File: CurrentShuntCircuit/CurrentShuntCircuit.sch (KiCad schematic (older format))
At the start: 48 parts, among them J1 Connection, J2 Connection, J3 Debug/UPDI, J4 Screw_Terminal_01x04, J5 Screw_Terminal_01x04, J6 ScrewTerminal, SW1 SW_DIP_x02, U1 TLP172GM, U2 ATtiny1614-SS, U3 INA228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

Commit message: Updated footprints
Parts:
- SW1: footprint CurrentShuntCircuit:XKBConnectivity_DSHP02TS-S_P1.27 -> Button_Switch_THT:SW_DIP_SPSTx02_Slide_6.7x6.64mm_W7.62mm_P2.54mm_LowProfile; LCSCStockCode C319052 -> C458081
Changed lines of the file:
@@
 F 0 "SW1" H 5835 7067 50  0000 C CNN
 F 1 "SW_DIP_x02" H 5835 6976 50  0000 C CNN
-F 2 "CurrentShuntCircuit:XKBConnectivity_DSHP02TS-S_P1.27" H 5835 6700 50  0001 C CNN
-F 3 "https://datasheet.lcsc.com/szlcsc/2002271742_XKB-Connectivity-DSHP02TS-S_C319052.pdf" H 5835 6700 50  0001 C CNN
-F 4 "C319052" H 5835 6700 50  0001 C CNN "LCSCStockCode"
+F 2 "Button_Switch_THT:SW_DIP_SPSTx02_Slide_6.7x6.64mm_W7.62mm_P2.54mm_LowProfile" H 5835 6700 50  0001 C CNN
+F 3 "https://datasheet.lcsc.com/szlcsc/2004251705_Korean-Hroparts-Elec-DS-02BP_C458081.pdf" H 5835 6700 50  0001 C CNN
+F 4 "C458081" H 5835 6700 50  0001 C CNN "LCSCStockCode"
 	1    5835 6700
 	1    0    0    -1

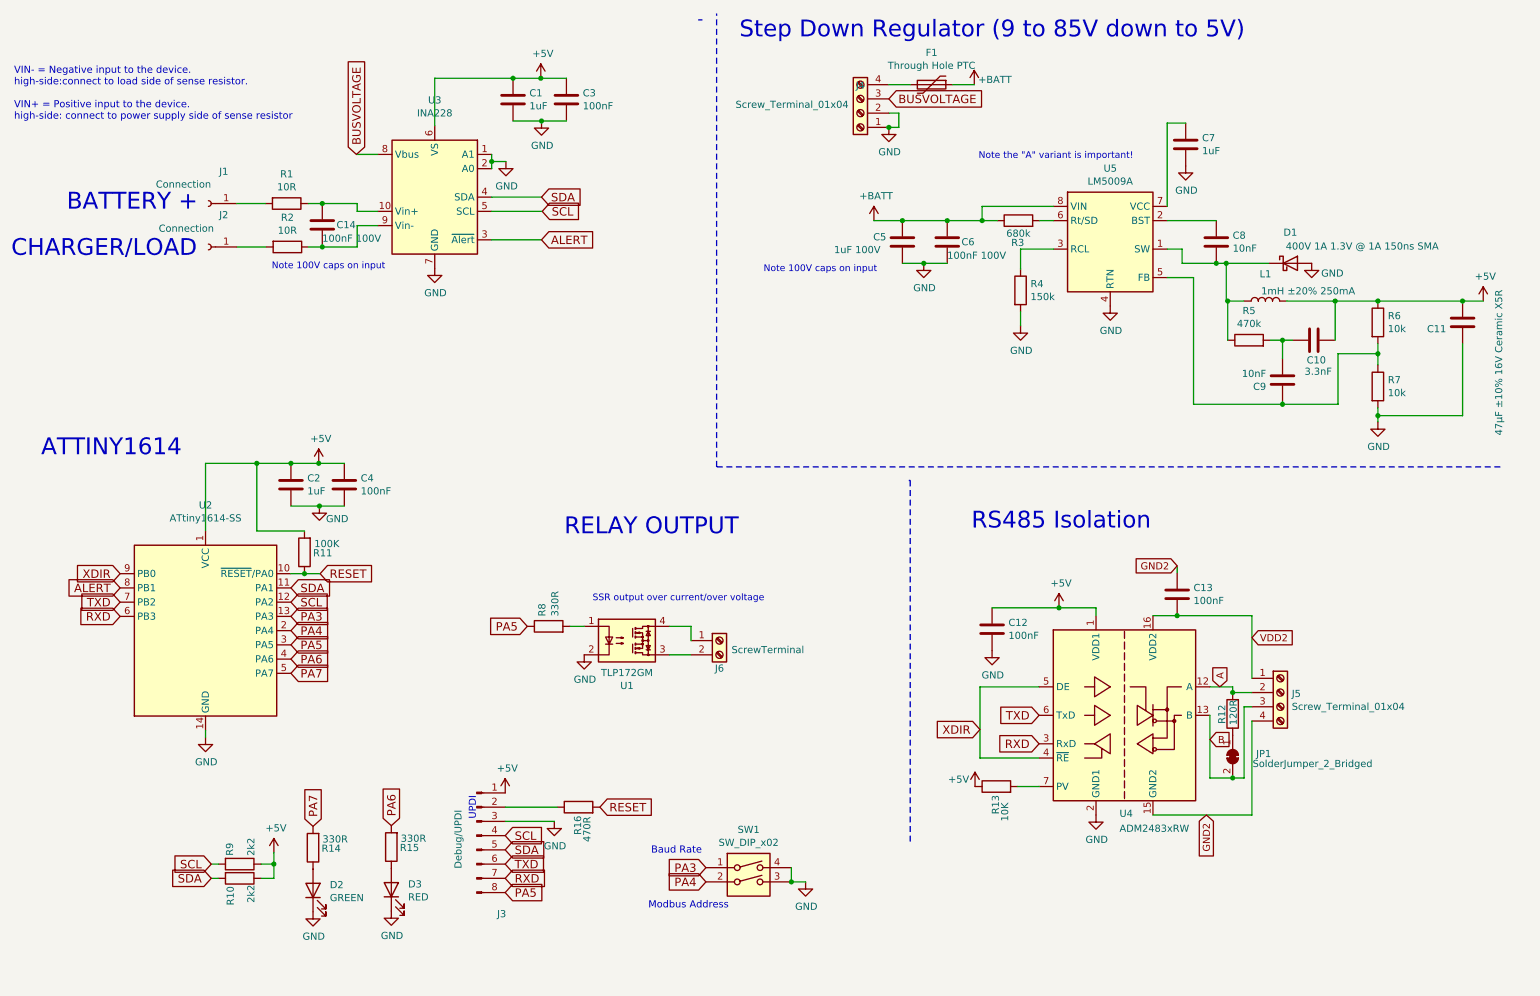
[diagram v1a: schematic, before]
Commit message: Tidy up and change i2c pull ups to 4k7
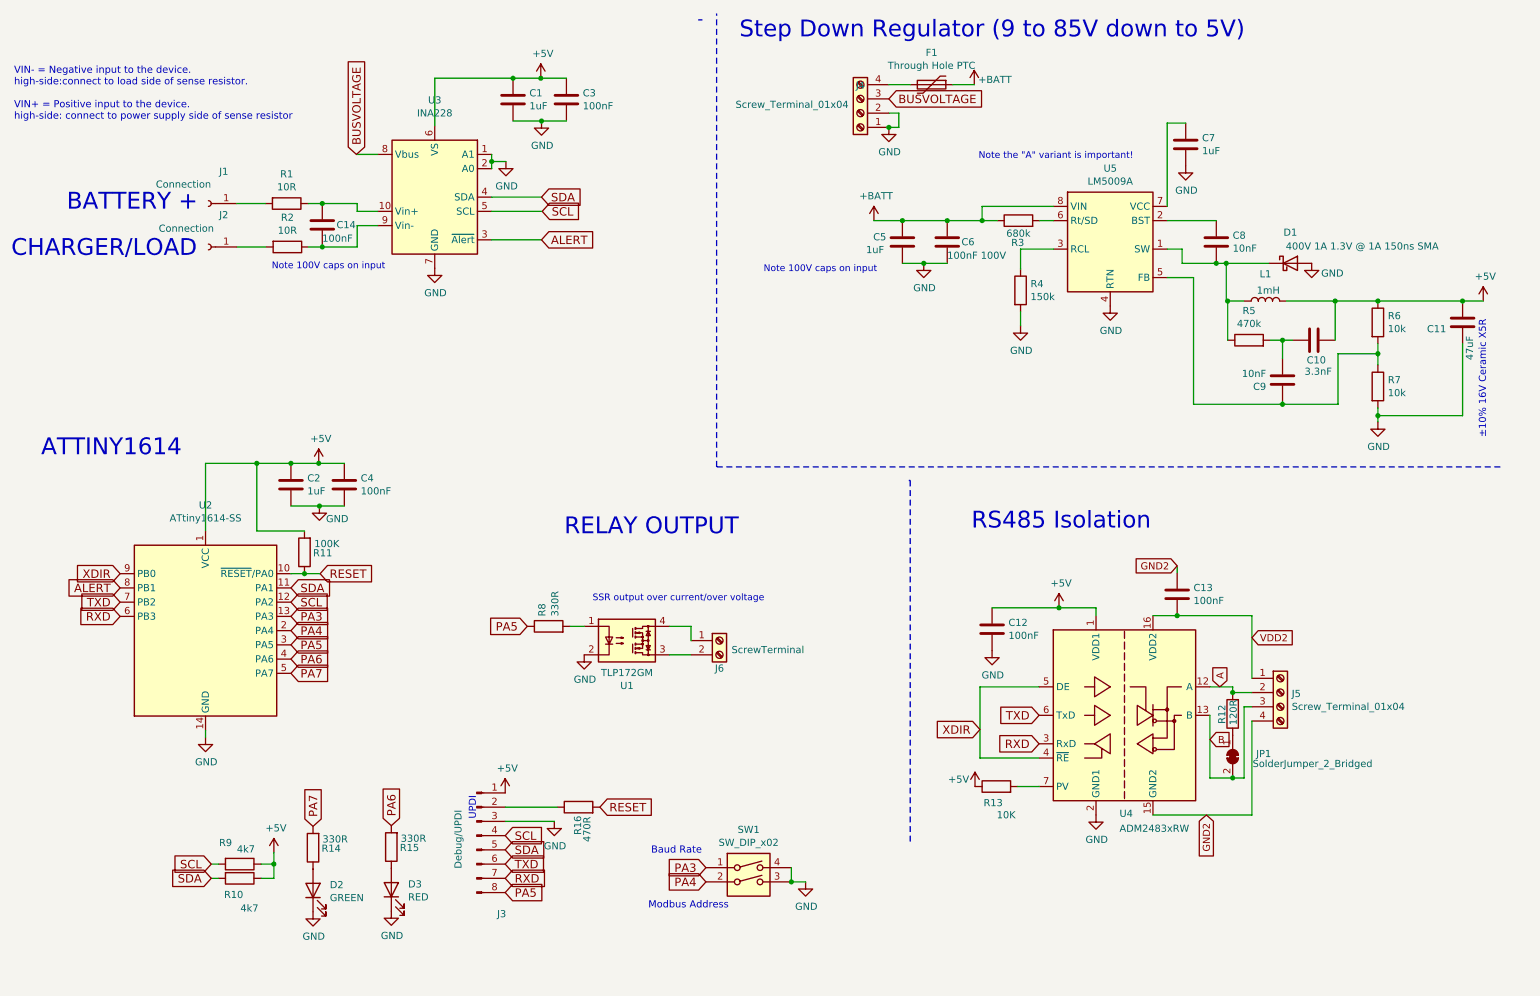
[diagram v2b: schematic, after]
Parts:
- C11: value 47µF ±10% 16V Ceramic X5R -> 47uF
- C14: value 100nF 100V -> 100nF
- C5: value 1uF 100V -> 1uF
- L1: value 1mH ±20% 250mA -> 1mH
- R10, R9: value 2k2 -> 4k7; LCSCStockCode C17520 -> C17673; PartNumber 0805W8F2201T5E -> 0805W8F4701T5E
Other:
- note added: "±10% 16V Ceramic X5R"
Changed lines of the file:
@@
 P 6915 2205
 F 0 "C5" H 6710 2240 50  0000 L CNN
-F 1 "1uF 100V" H 6435 2150 50  0000 L CNN
+F 1 "1uF" H 6660 2150 50  0000 L CNN
 F 2 "Capacitor_SMD:C_1206_3216Metric" H 6953 2055 50  0001 C CNN
 F 3 "https://datasheet.lcsc.com/szlcsc/Samsung-Electro-Mechanics-CL31B105KCHNNNE_C13832.pdf" H 6915 2205 50  0001 C CNN
@@
 P 9465 2620
 F 0 "L1" V 9655 2620 50  0000 C CNN
-F 1 "1mH ±20% 250mA" V 9535 2320 50  0000 C CNN
+F 1 "1mH" V 9540 2600 50  0000 C CNN
 F 2 "Inductor_SMD:L_TDK_SLF7045" H 9465 2620 50  0001 C CNN
 F 3 "" H 9465 2620 50  0001 C CNN
@@
 P 10850 2770
 F 0 "C11" H 10965 2816 50  0000 L CNN
-F 1 "47µF ±10% 16V Ceramic X5R" V 10595 2540 50  0000 L CNN
+F 1 "47uF" V 10800 2865 50  0000 L CNN
 F 2 "Capacitor_SMD:C_1210_3225Metric" H 10888 2620 50  0001 C CNN
 F 3 "https://search.murata.co.jp/Ceramy/image/img/A01X/G101/ENG/GRM32ER61C476KE15-01.pdf" H 10850 2770 50  0001 C CNN
@@
 U 1 1 603EC275
 P 2260 6575
-F 0 "R9" H 2110 6505 50  0000 L CNN
-F 1 "2k2" H 2075 6655 50  0000 L CNN
+F 0 "R9" V 2110 6430 50  0000 L CNN
+F 1 "4k7" V 2155 6555 50  0000 L CNN
 F 2 "Resistor_SMD:R_0805_2012Metric" V 2190 6575 50  0001 C CNN
 F 3 "~" H 2260 6575 50  0001 C CNN
-F 4 "C17520" H 2260 6575 50  0001 C CNN "LCSCStockCode"
-F 5 "0805W8F2201T5E" H 2260 6575 50  0001 C CNN "PartNumber"
+F 4 "C17673" H 2260 6575 50  0001 C CNN "LCSCStockCode"
+F 5 "0805W8F4701T5E" H 2260 6575 50  0001 C CNN "PartNumber"
 	1    2260 6575
 	0    1    1    0
@@
 U 1 1 603ECB25
 P 2260 6675
-F 0 "R10" H 2315 6610 50  0000 L CNN
-F 1 "2k2" H 2305 6755 50  0000 L CNN
+F 0 "R10" V 2375 6565 50  0000 L CNN
+F 1 "4k7" V 2470 6680 50  0000 L CNN
 F 2 "Resistor_SMD:R_0805_2012Metric" V 2190 6675 50  0001 C CNN
 F 3 "~" H 2260 6675 50  0001 C CNN
-F 4 "C17520" H 2260 6675 50  0001 C CNN "LCSCStockCode"
-F 5 "0805W8F2201T5E" H 2260 6675 50  0001 C CNN "PartNumber"
+F 4 "C17673" H 2260 6675 50  0001 C CNN "LCSCStockCode"
+F 5 "0805W8F4701T5E" H 2260 6675 50  0001 C CNN "PartNumber"
 	1    2260 6675
 	0    1    1    0
@@
 U 1 1 6044C50D
 P 7575 6030
-F 0 "R13" H 7380 6035 50  0000 L CNN
-F 1 "10K" H 7330 5970 50  0000 L CNN
+F 0 "R13" V 7460 5985 50  0000 L CNN
+F 1 "10K" V 7375 5895 50  0000 L CNN
 F 2 "Resistor_SMD:R_0805_2012Metric" V 7505 6030 50  0001 C CNN
 F 3 "~" H 7575 6030 50  0001 C CNN
@@
 P 2840 2085
 F 0 "C14" H 2940 2085 50  0000 L CNN
-F 1 "100nF 100V" H 2840 1990 50  0000 L CNN
+F 1 "100nF" H 2840 1990 50  0000 L CNN
 F 2 "Capacitor_SMD:C_0805_2012Metric" H 2878 1935 50  0001 C CNN
 F 3 "https://datasheet.lcsc.com/szlcsc/2008131833_KEMET-C0805C104K1RECAUTO_C696367.pdf" H 2840 2085 50  0001 C CNN
@@
 Wire Wire Line
 	4125 6275 4470 6275
+Text Notes 11020 3585 1    50   ~ 0
+±10% 16V Ceramic X5R
 $EndSCHEMATC

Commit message: Update CurrentShuntCircuit.sch
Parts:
- C14: value 100nF -> 100nF 100V
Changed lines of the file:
@@
 P 2840 2085
 F 0 "C14" H 2940 2085 50  0000 L CNN
-F 1 "100nF" H 2840 1990 50  0000 L CNN
+F 1 "100nF 100V" H 2840 1990 50  0000 L CNN
 F 2 "Capacitor_SMD:C_0805_2012Metric" H 2878 1935 50  0001 C CNN
 F 3 "https://datasheet.lcsc.com/szlcsc/2008131833_KEMET-C0805C104K1RECAUTO_C696367.pdf" H 2840 2085 50  0001 C CNN

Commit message: Update JLCPCB code
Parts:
- U4: LCSCStockCode C9637 -> C386280
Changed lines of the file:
@@
 F 3 "https://www.analog.com/media/en/technical-documentation/data-sheets/adm2483.pdf" H 7725 5580 50  0001 C CNN
 F 4 "ADM2483BRWZ-REEL" H 8475 5530 50  0001 C CNN "PartNumber"
-F 5 "C9637" H 8475 5530 50  0001 C CNN "LCSCStockCode"
+F 5 "C386280" H 8475 5530 50  0001 C CNN "LCSCStockCode"
 	1    8475 5530
 	1    0    0    -1

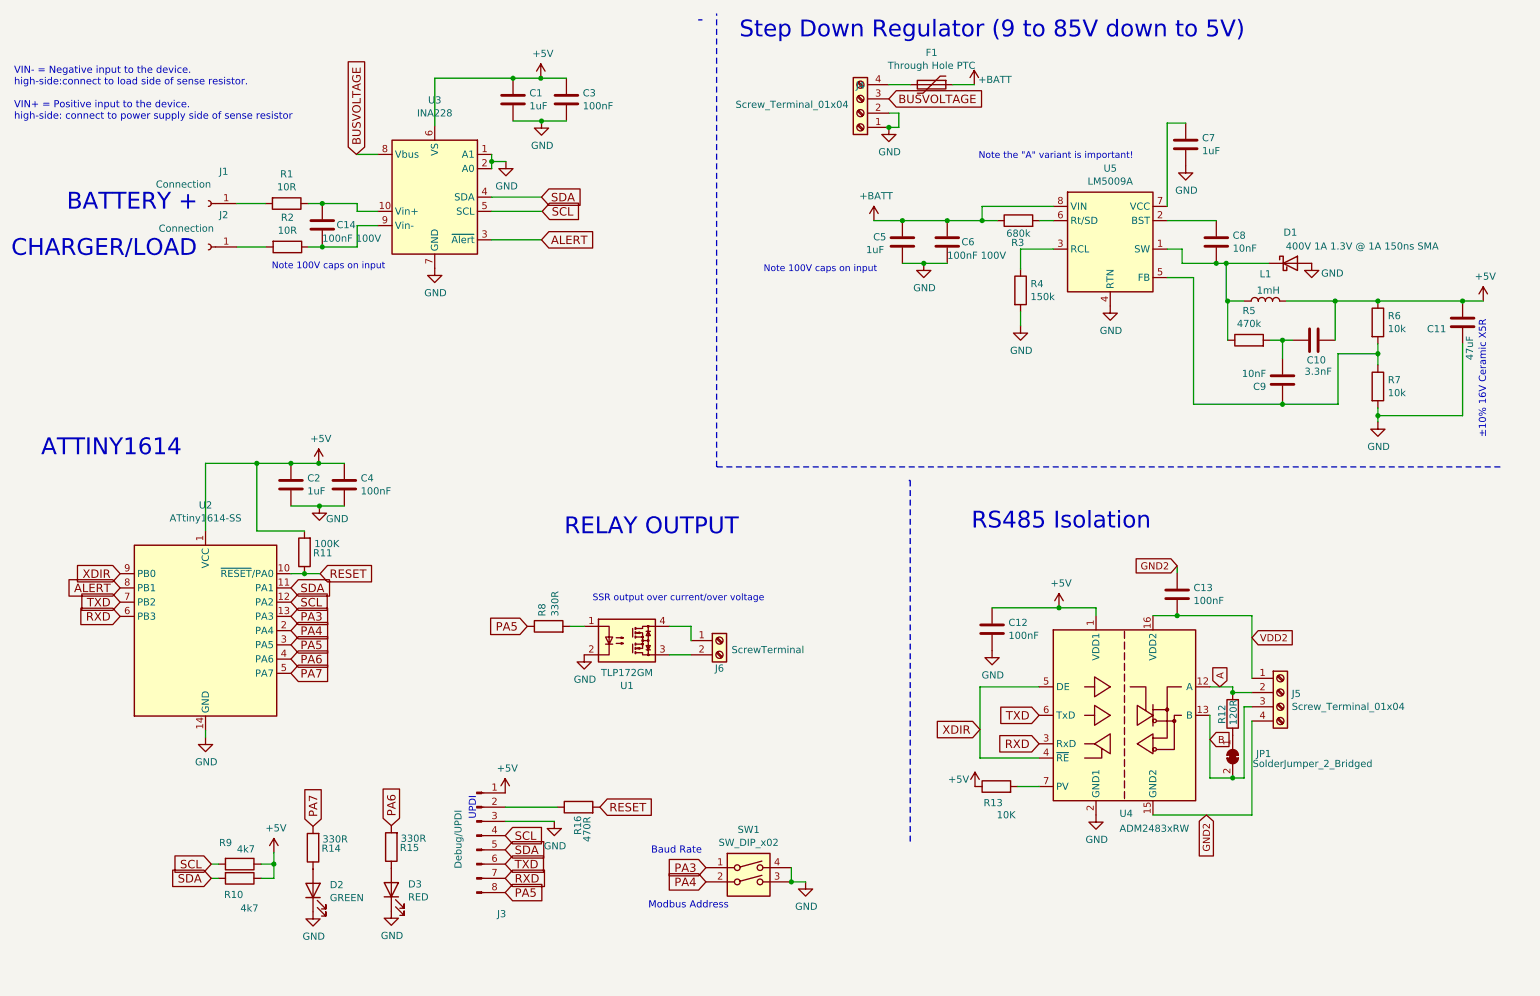
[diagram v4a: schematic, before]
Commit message: Change optoisolator
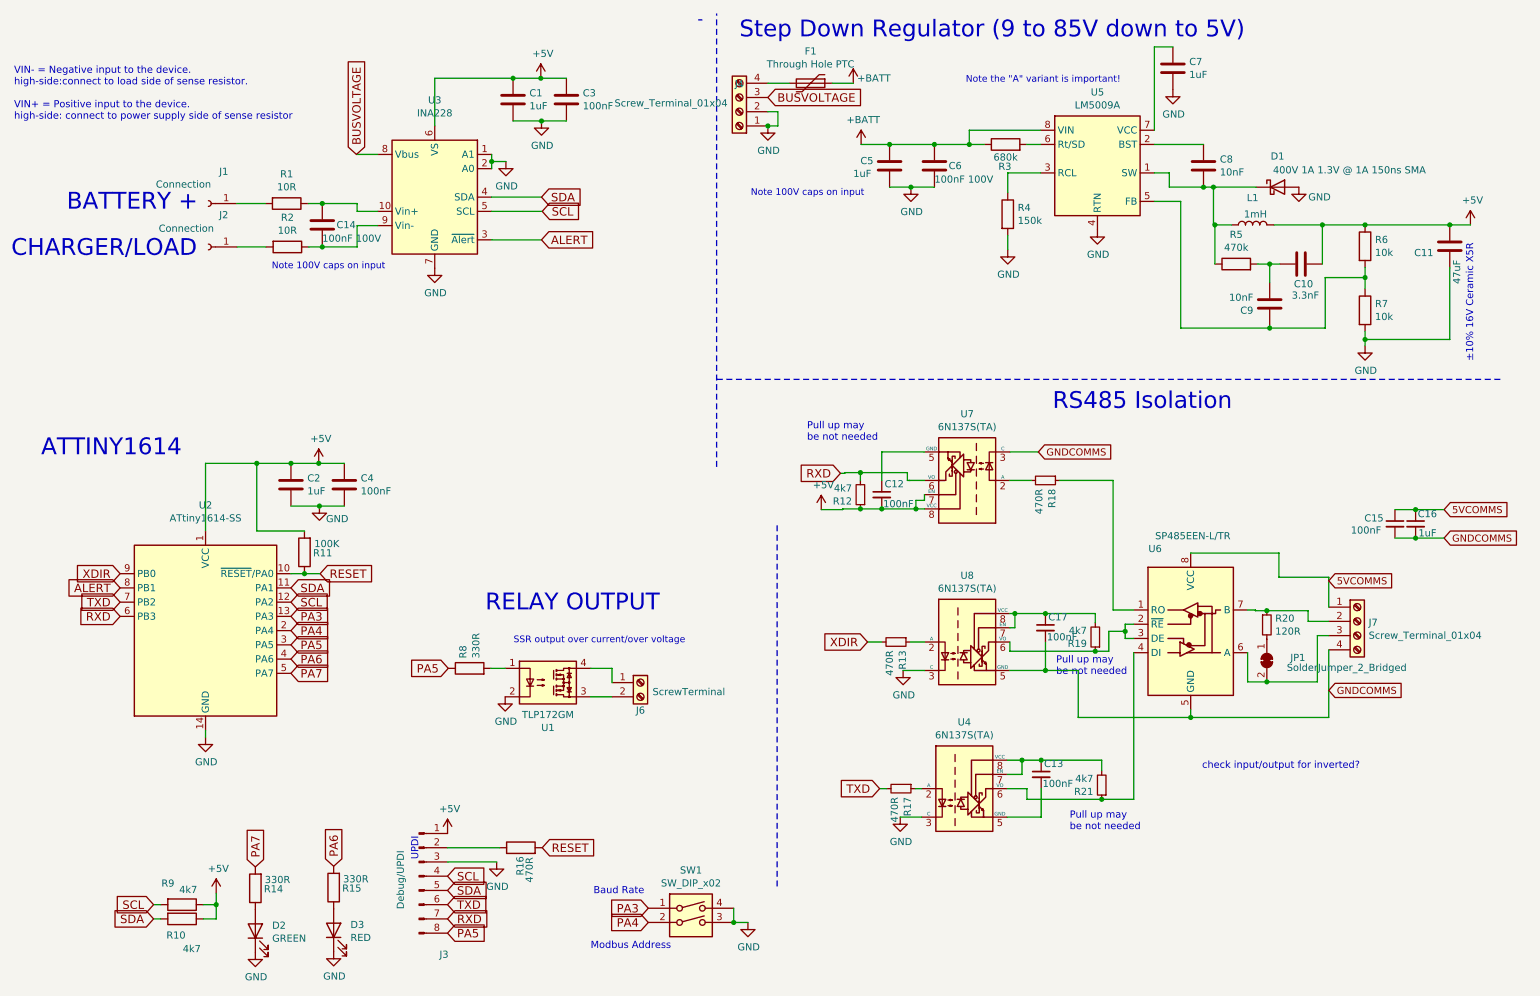
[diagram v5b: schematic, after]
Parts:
- removed C12, C13: 100nF, Capacitor_SMD:C_0805_2012Metric, symbol Device:C
- removed J5: Screw_Terminal_01x04, CurrentShuntCircuit:Terminal-Block_3.81_4P_LCSC_C395880, symbol Connector:Screw_Terminal_01x04
- removed R12: 120R, Resistor_SMD:R_0805_2012Metric, symbol Device:R
- removed R13: 10K, Resistor_SMD:R_0805_2012Metric, symbol Device:R
- removed U4: ADM2483xRW, Package_SO:SOIC-16W_7.5x10.3mm_P1.27mm, symbol Interface_UART:ADM2483xRW
- added C12, C13, C15, C17: 100nF, Capacitor_SMD:C_0805_2012Metric, symbol Device:C_Small
- added C16: 1uF, Capacitor_SMD:C_0805_2012Metric, symbol Device:C_Small
- added J7: Screw_Terminal_01x04, CurrentShuntCircuit:Terminal-Block_3.81_4P_LCSC_C395880, symbol Connector:Screw_Terminal_01x04
- added R12, R19, R21: 4k7, Resistor_SMD:R_0805_2012Metric, symbol Device:R_Small
- added R13, R17, R18: 470R, Resistor_SMD:R_0805_2012Metric, symbol Device:R_Small
- added R20: 120R, Resistor_SMD:R_0805_2012Metric, symbol Device:R_Small
- added U4, U7, U8: 6N137S(TA), Package_SO:SOP-8_6.62x9.15mm_P2.54mm, symbol Isolator:6N137
- added U6: SP485EEN-L/TR, Package_SO:SOIC-8_3.9x4.9mm_P1.27mm, symbol Interface_UART:MAX485E
- J3: LCSCStockCode (none) -> C124381
- U3: LCSCStockCode (none) -> C2887910
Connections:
- net +5V: now also C12.2, R12.1, U7.7 (EN), U7.8 (VCC)
- net GND: now also U4.3 (C), U8.3 (C)
- net RXD: now also R12.2, U7.6 (VO)
- net TXD: now also R17.2
- net XDIR: now also R13.2
- net at JP1.1 (A): now also R20.2
- net B: no longer names the net of JP1.2 (B)
- net B: now also J7.3 (Pin_3), U6.6 (A)
- new net: R18.1, U6.1 (RO)
- new net: R19.1, U6.2 (~RE), U6.3 (DE), U8.6 (VO)
- new net: R21.1, U4.6 (VO), U6.4 (DI)
- new net: J7.2 (Pin_2), R20.1, U6.7 (B)
- new net: R13.1, U8.2 (A)
- new net: C17.1, R19.2, U8.7 (EN), U8.8 (VCC)
- new net: R17.1, U4.2 (A)
- new net: C13.2, U4.5 (GND)
- new net: C13.1, R21.2, U4.7 (EN), U4.8 (VCC)
- new net: R18.2, U7.2 (A)
- new net: C12.1, U7.5 (GND)
- new net 5VCOMMS: C15.1, C16.1, J7.1 (Pin_1), U6.8 (VCC)
- new net GNDCOMMS: C15.2, C16.2, C17.2, J7.4 (Pin_4), U6.5 (GND), U7.3 (C), U8.5 (GND)
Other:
- note added: "Pull up may \nbe not needed"
- note added: "check input/output for inverted?"
- moved on the sheet: C10, C11, C5, C6, C7, C8, C9, D1, D2, D3, F1, J3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
